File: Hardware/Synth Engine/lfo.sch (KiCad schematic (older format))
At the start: 29 parts, among them SW1 SW_DPDT_x2, U4 TL074, U5 TL074

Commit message: connect control board to main synth schem pages
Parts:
- removed RV17: 10kA, Potentiometers:Potentiometer_Bourns_PTV09A-1_Horizontal, symbol POT
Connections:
- net LFO_in: now reaches R82.1
- net LFO_out: now reaches C72.1, U4.6 (-)
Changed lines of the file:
@@
-$EndComp
-$Comp
-L POT RV17
-U 1 1 5C380212
-P 2500 3600
-F 0 "RV17" V 2325 3600 50  0000 C CNN
-F 1 "10kA" V 2400 3600 50  0000 C CNN
-F 2 "Potentiometers:Potentiometer_Bourns_PTV09A-1_Horizontal" H 2500 3600 50  0001 C CNN
-F 3 "" H 2500 3600 50  0001 C CNN
-	1    2500 3600
-	0    1    1    0
 $EndComp
 $Comp
@@
 	1850 3600 1950 3600
 Wire Wire Line
-	2250 3600 2350 3600
+	2250 3600 2300 3600
 $Comp
 L R R89
@@
 Text GLabel 5250 4600 1    60   Input ~ 0
 VREF
-Wire Wire Line
-	2500 3750 2300 3750
-Wire Wire Line
-	2300 3750 2300 3600
-Connection ~ 2300 3600
+Text HLabel 2300 3400 2    60   Output ~ 0
+LFO_in
+Text HLabel 2650 3500 0    60   Input ~ 0
+LFO_out
+Wire Wire Line
+	2300 3600 2300 3400
+Wire Wire Line
+	2650 3500 2650 3600
 $EndSCHEMATC

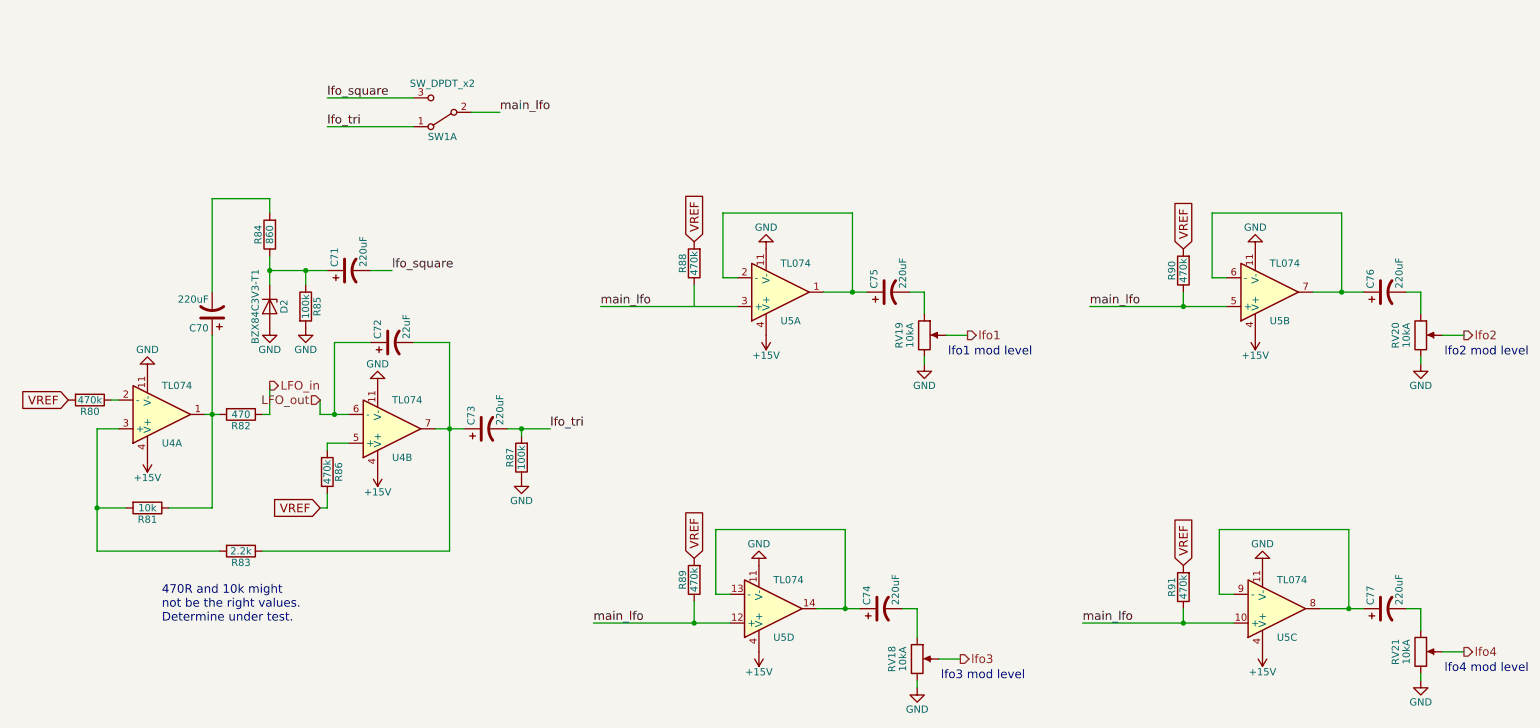
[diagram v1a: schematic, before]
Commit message: add connectors for capsense buttons and LFO shape switch
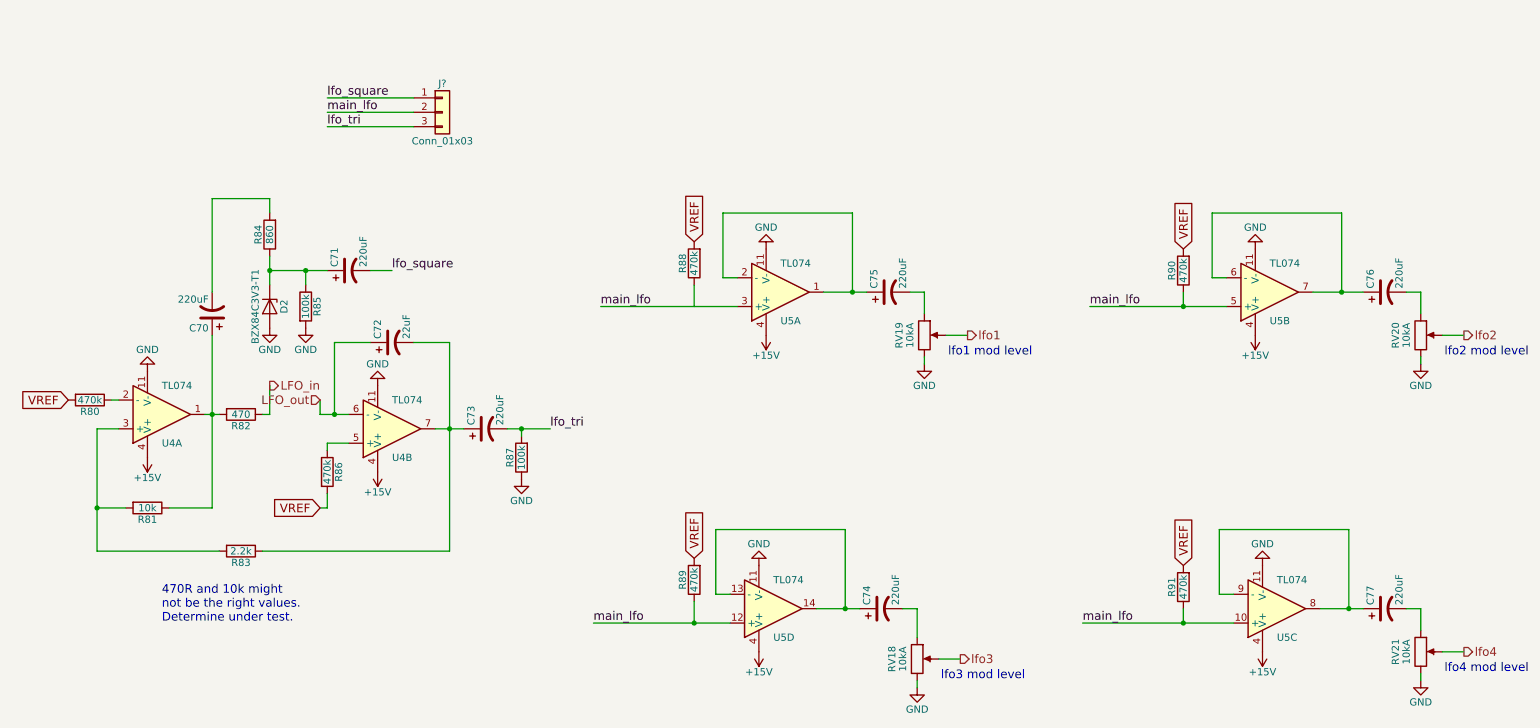
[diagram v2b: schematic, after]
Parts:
- removed SW1: SW_DPDT_x2, SparkFun-Electromechanical:SWITCH-SPDT, symbol SW_DPDT_x2
- added J?: Conn_01x03, symbol Conn_01x03
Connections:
- net lfo_square: now also J?.1 (Pin_1)
- net lfo_tri: now also J?.3 (Pin_3)
- net main_lfo: now also J?.2 (Pin_2)
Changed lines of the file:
@@
 Text Label 4250 3700 0    60   ~ 0
 lfo_tri
-$Comp
-L SW_DPDT_x2 SW1
-U 1 1 5C38FB5B
-P 3500 1500
-F 0 "SW1" H 3500 1670 50  0000 C CNN
-F 1 "SW_DPDT_x2" H 3500 1300 50  0000 C CNN
-F 2 "SparkFun-Electromechanical:SWITCH-SPDT" H 3500 1500 50  0001 C CNN
-F 3 "" H 3500 1500 50  0001 C CNN
-	1    3500 1500
-	-1   0    0    1
-$EndComp
 Text Label 2700 1600 0    60   ~ 0
 lfo_tri
 Text Label 2700 1400 0    60   ~ 0
 lfo_square
-Text Label 3900 1500 0    60   ~ 0
+Text Label 2700 1500 0    60   ~ 0
 main_lfo
 Text Notes 1550 5050 0    60   ~ 0
@@
 	10200 4950 10300 4950
 Wire Wire Line
-	9600 4950 9900 4950
+	9600 4950 9800 4950
+Wire Wire Line
+	9800 4950 9900 4950
 Wire Wire Line
 	10200 2750 10300 2750
 Wire Wire Line
-	9550 2750 9900 2750
+	9550 2750 9750 2750
+Wire Wire Line
+	9750 2750 9900 2750
 Wire Wire Line
 	6700 4950 6800 4950
 Wire Wire Line
-	6100 4950 6400 4950
+	6100 4950 6300 4950
+Wire Wire Line
+	6300 4950 6400 4950
 Wire Wire Line
 	6750 2750 6850 2750
 Wire Wire Line
-	6150 2750 6450 2750
+	6150 2750 6350 2750
+Wire Wire Line
+	6350 2750 6450 2750
 Connection ~ 8650 5050
 Wire Wire Line
@@
 	9800 4950 9800 4400
 Wire Wire Line
-	7950 5050 9000 5050
+	7950 5050 8650 5050
+Wire Wire Line
+	8650 5050 9000 5050
 Connection ~ 6300 4950
 Wire Wire Line
@@
 	6300 4950 6300 4400
 Wire Wire Line
-	4550 5050 5500 5050
+	4550 5050 5250 5050
+Wire Wire Line
+	5250 5050 5500 5050
 Connection ~ 9750 2750
 Wire Wire Line
@@
 	9750 2750 9750 2200
 Wire Wire Line
-	8000 2850 8950 2850
+	8000 2850 8650 2850
+Wire Wire Line
+	8650 2850 8950 2850
 Connection ~ 6350 2750
 Wire Wire Line
@@
 	2550 2600 2550 2700
 Wire Wire Line
-	3900 1500 3700 1500
-Wire Wire Line
 	2700 1400 3300 1400
 Wire Wire Line
@@
 Connection ~ 2300 2600
 Wire Wire Line
-	2300 2600 2700 2600
+	2300 2600 2550 2600
+Wire Wire Line
+	2550 2600 2700 2600
 Wire Wire Line
 	2300 2100 2300 2200
@@
 	1900 2100 2300 2100
 Wire Wire Line
-	2300 2500 2300 2700
+	2300 2500 2300 2600
+Wire Wire Line
+	2300 2600 2300 2700
 Wire Wire Line
 	2700 3800 2850 3800
 Wire Wire Line
-	2650 3600 2850 3600
-Wire Wire Line
-	3450 3700 3650 3700
+	2650 3600 2750 3600
+Wire Wire Line
+	2750 3600 2850 3600
+Wire Wire Line
+	3450 3700 3550 3700
+Wire Wire Line
+	3550 3700 3650 3700
 Wire Wire Line
 	1250 3700 1100 3700
@@
 Connection ~ 4050 3700
 Wire Wire Line
-	3950 3700 4250 3700
+	3950 3700 4050 3700
+Wire Wire Line
+	4050 3700 4250 3700
 Wire Wire Line
 	4050 3750 4050 3700
@@
 	3550 4550 2250 4550
 Wire Wire Line
-	1100 3700 1100 4550
+	1100 3700 1100 4250
+Wire Wire Line
+	1100 4250 1100 4550
 Wire Wire Line
 	1300 4250 1100 4250
@@
 	1900 4250 1600 4250
 Wire Wire Line
-	1900 3050 1900 4250
+	1900 3050 1900 3600
+Wire Wire Line
+	1900 3600 1900 4250
 Wire Wire Line
 	2700 3850 2700 3800
@@
 	3550 3100 3300 3100
 Wire Wire Line
-	3550 3100 3550 4550
-Wire Wire Line
-	1850 3600 1950 3600
+	3550 3100 3550 3700
+Wire Wire Line
+	3550 3700 3550 4550
+Wire Wire Line
+	1850 3600 1900 3600
+Wire Wire Line
+	1900 3600 1950 3600
 Wire Wire Line
 	2250 3600 2300 3600
@@
 Wire Wire Line
 	2650 3500 2650 3600
+$Comp
+L Conn_01x03 J?
+U 1 1 5C5E25FE
+P 3500 1500
+F 0 "J?" H 3500 1700 50  0000 C CNN
+F 1 "Conn_01x03" H 3500 1300 50  0000 C CNN
+F 2 "" H 3500 1500 50  0001 C CNN
+F 3 "" H 3500 1500 50  0001 C CNN
+	1    3500 1500
+	1    0    0    -1
+$EndComp
+Wire Wire Line
+	2700 1500 3300 1500
 $EndSCHEMATC

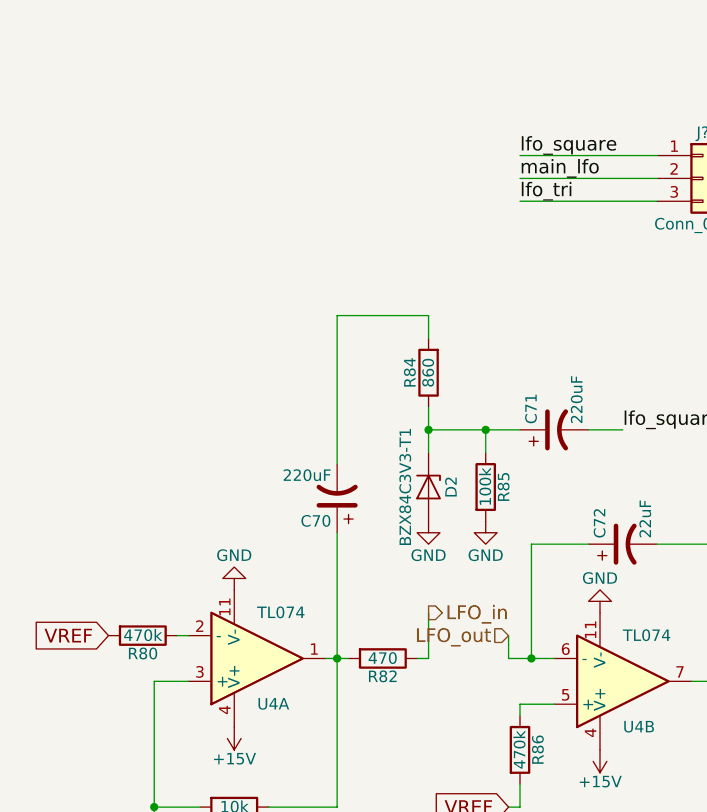
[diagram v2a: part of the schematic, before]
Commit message: remove extraneous net labels
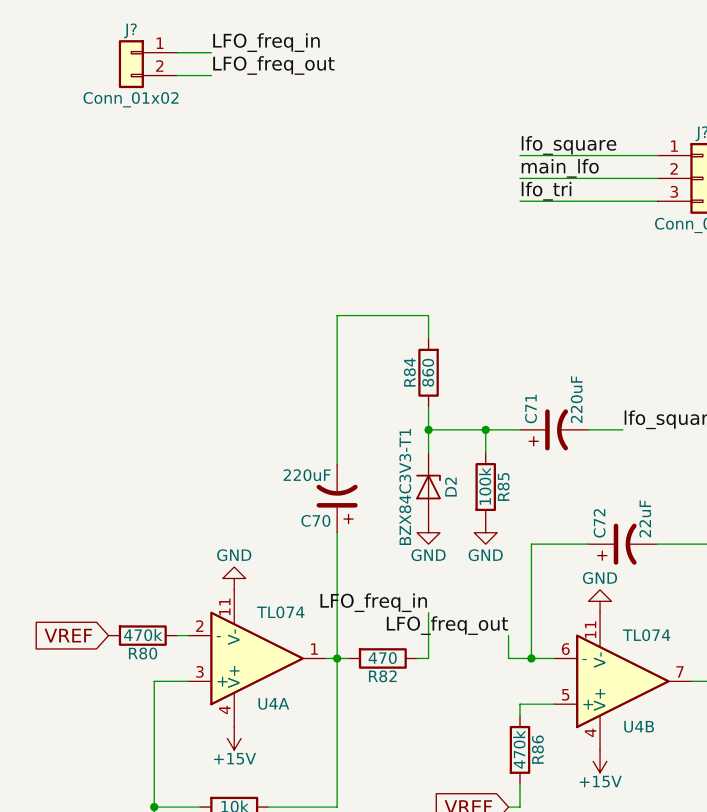
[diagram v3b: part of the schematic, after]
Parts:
- added J?: Conn_01x02, symbol Conn_01x02
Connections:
- net LFO_in renamed LFO_freq_in
- net LFO_freq_in: now also J?.1 (Pin_1)
- net LFO_out renamed LFO_freq_out
- net LFO_freq_out: now also J?.2 (Pin_2)
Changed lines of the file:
@@
 Text GLabel 5250 4600 1    60   Input ~ 0
 VREF
-Text HLabel 2300 3400 2    60   Output ~ 0
-LFO_in
-Text HLabel 2650 3500 0    60   Input ~ 0
-LFO_out
 Wire Wire Line
 	2300 3600 2300 3400
@@
 Wire Wire Line
 	2700 1500 3300 1500
+$Comp
+L Conn_01x02 J?
+U 1 1 5C5E39A1
+P 1000 950
+F 0 "J?" H 1000 1050 50  0000 C CNN
+F 1 "Conn_01x02" H 1000 750 50  0000 C CNN
+F 2 "" H 1000 950 50  0001 C CNN
+F 3 "" H 1000 950 50  0001 C CNN
+	1    1000 950
+	-1   0    0    -1
+$EndComp
+Wire Wire Line
+	1200 950  1350 950
+Wire Wire Line
+	1350 1050 1200 1050
+Text Label 1350 950  0    60   ~ 0
+LFO_freq_in
+Text Label 1350 1050 0    60   ~ 0
+LFO_freq_out
+Text Label 2300 3400 2    60   ~ 0
+LFO_freq_in
+Text Label 2650 3500 2    60   ~ 0
+LFO_freq_out
 $EndSCHEMATC
